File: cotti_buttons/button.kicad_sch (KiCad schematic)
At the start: 5 parts, among them SW1 SW_Push_Dual, U1 Invert Schmitt

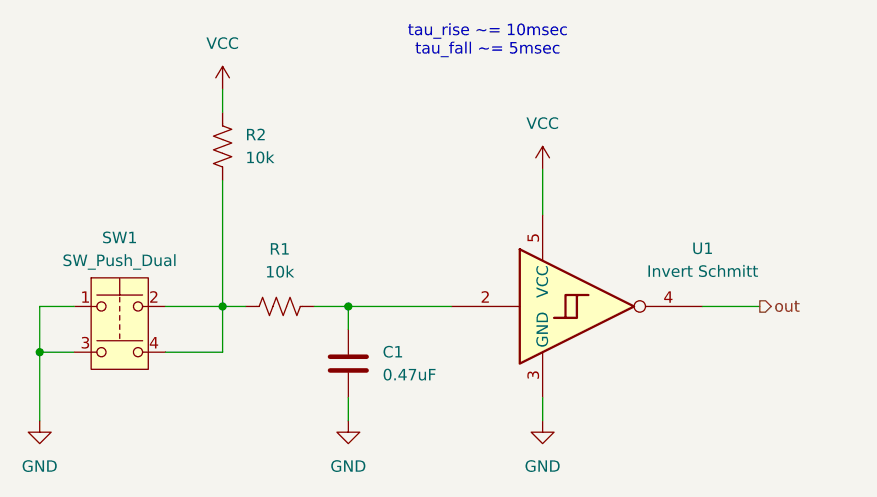
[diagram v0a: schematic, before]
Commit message: feat: cotti uttons with new libs
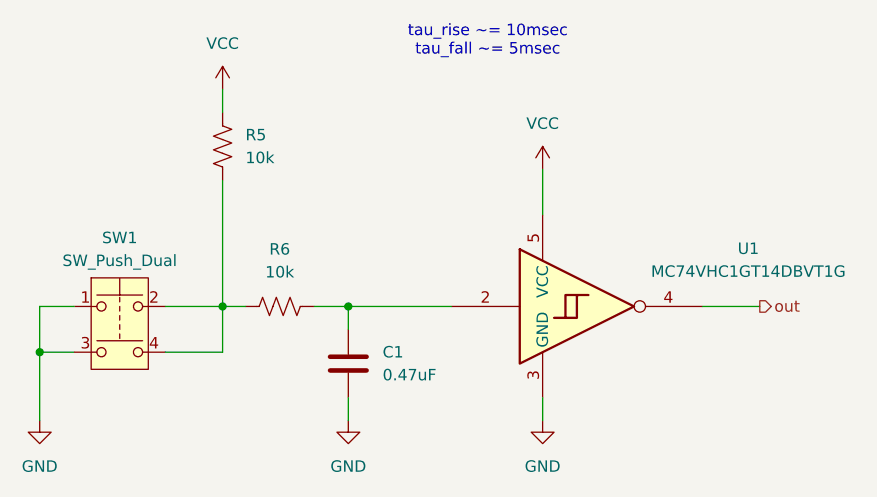
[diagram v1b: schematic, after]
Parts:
- removed SW1: SW_Push_Dual, Button_Switch_THT:SW_PUSH_6mm_H5mm, symbol Switch:SW_Push_Dual
- removed U1: Invert Schmitt, Package_TO_SOT_SMD:SC-74A-5_1.55x2.9mm_P0.95mm, symbol 74xGxx:74AHC1G14
- added SW1: SW_Push_Dual, Button_Switch_THT:SW_PUSH_6mm_H5mm, symbol cotti_switch:SW_Push_Dual
- added U1: MC74VHC1GT14DBVT1G, Package_TO_SOT_SMD:SC-74A-5_1.55x2.9mm_P0.95mm, symbol cotti_ic:inverter_schmitt_input
- renumbered R2 to R5, R1 to R6
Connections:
- net GND: now also SW1.1, SW1.3, U1.3 (GND)
- net VCC: now also U1.5 (VCC)
- net out: now also U1.4
- net at C1.1, R6.2: now also U1.2
- net at R5.2, R6.1: now also SW1.2, SW1.4
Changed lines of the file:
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@@
-	)
-	(symbol
-		(lib_id "74xGxx:74AHC1G14")
-		(at 173.99 97.79 0)
-		(unit 1)
-		(exclude_from_sim no)
-		(in_bom yes)
-		(on_board yes)
-		(dnp no)
-		(fields_autoplaced yes)
-		(property "Reference" "U1"
-			(at 186.69 91.3698 0)
-			(effects
-				(font
-					(size 1.27 1.27)
-				)
-			)
-		)
-		(property "Value" "Invert Schmitt"
-			(at 186.69 93.9098 0)
-			(effects
-				(font
-					(size 1.27 1.27)
-				)
-			)
-		)
-		(property "Footprint" "Package_TO_SOT_SMD:SC-74A-5_1.55x2.9mm_P0.95mm"
-			(at 173.99 97.79 0)
-			(effects
-				(font
-					(size 1.27 1.27)
-				)
-				(hide yes)
-			)
-		)
-		(property "Datasheet" "https://www.onsemi.com/pdf/datasheet/mc74vhc1g14-d.pdf"
-			(at 173.99 104.14 0)
-			(effects
-				(font
-					(size 1.27 1.27)
-				)
-				(justify left)
-				(hide yes)
-			)
-		)
-		(property "Description" "Inverter IC 1 Channel Schmitt Trigger SC-74A"
-			(at 173.99 97.79 0)
-			(effects
-				(font
-					(size 1.27 1.27)
-				)
-				(hide yes)
-			)
-		)
-		(property "Digikey" "https://www.digikey.com/en/products/detail/onsemi/MC74VHC1GT14DBVT1G/10064713"
-			(at 173.99 97.79 0)
-			(effects
-				(font
-					(size 1.27 1.27)
-				)
-				(hide yes)
-			)
-		)
-		(property "Digikey P/N" "488-MC74VHC1GT14DBVT1GCT-ND"
-			(at 173.99 97.79 0)
-			(effects
-				(font
-					(size 1.27 1.27)
-				)
-				(hide yes)
-			)
-		)
-		(property "Mfr." "onsemi"
-			(at 173.99 97.79 0)
-			(effects
-				(font
-					(size 1.27 1.27)
-				)
-				(hide yes)
-			)
-		)
-		(property "Mfr. P/N" "MC74VHC1GT14DBVT1G"
-			(at 173.99 97.79 0)
-			(effects
-				(font
-					(size 1.27 1.27)
-				)
-				(hide yes)
-			)
-		)
-		(pin "1"
-		)
-		(pin "4"
-		)
-		(pin "3"
-		)
-		(pin "2"
-		)
-		(pin "5"
-		)
-		(instances
-			(project "cotti_buttons"
-				(path "/673b428a-a10a-4837-8ece-1839a9ec4aa8/34456084-0fea-4792-bf42-1a35ca3e3257"
-					(reference "U1")
-					(unit 1)
-				)
-				(path "/673b428a-a10a-4837-8ece-1839a9ec4aa8/408eaa88-2d34-400c-9210-e43e7ee9c2ee"
-					(reference "U3")
-					(unit 1)
-				)
-				(path "/673b428a-a10a-4837-8ece-1839a9ec4aa8/5fd56874-714f-4976-9abd-9de7879c2a1d"
-					(reference "U4")
-					(unit 1)
-				)
-				(path "/673b428a-a10a-4837-8ece-1839a9ec4aa8/7882fe45-d505-43e1-b077-86683bbfd833"
-					(reference "U2")
-					(unit 1)
-				)
-			)
-		)
 	)
 	(symbol
@@
 		(dnp no)
 		(fields_autoplaced yes)
-		(property "Reference" "#PWR05"
+		(property "Reference" "#PWR03"
 			(at 113.03 116.84 0)
 			(effects
@@
 			(project "cotti_buttons"
 				(path "/673b428a-a10a-4837-8ece-1839a9ec4aa8/34456084-0fea-4792-bf42-1a35ca3e3257"
-					(reference "#PWR05")
+					(reference "#PWR03")
 					(unit 1)
 				)
@@
 		(dnp no)
 		(fields_autoplaced yes)
-		(property "Reference" "#PWR04"
+		(property "Reference" "#PWR05"
 			(at 147.32 116.84 0)
 			(effects
@@
 			(project ""
 				(path "/673b428a-a10a-4837-8ece-1839a9ec4aa8/34456084-0fea-4792-bf42-1a35ca3e3257"
-					(reference "#PWR04")
+					(reference "#PWR05")
 					(unit 1)
 				)
@@
 		(on_board yes)
 		(dnp no)
-		(property "Reference" "R2"
+		(property "Reference" "R5"
 			(at 135.89 78.7399 0)
 			(effects
@@
 			(project "cotti_buttons"
 				(path "/673b428a-a10a-4837-8ece-1839a9ec4aa8/34456084-0fea-4792-bf42-1a35ca3e3257"
-					(reference "R2")
+					(reference "R5")
 					(unit 1)
 				)
 				(path "/673b428a-a10a-4837-8ece-1839a9ec4aa8/408eaa88-2d34-400c-9210-e43e7ee9c2ee"
-					(reference "R6")
+					(reference "R9")
 					(unit 1)
 				)
 				(path "/673b428a-a10a-4837-8ece-1839a9ec4aa8/5fd56874-714f-4976-9abd-9de7879c2a1d"
-					(reference "R8")
+					(reference "R11")
 					(unit 1)
 				)
 				(path "/673b428a-a10a-4837-8ece-1839a9ec4aa8/7882fe45-d505-43e1-b077-86683bbfd833"
-					(reference "R4")
+					(reference "R7")
 					(unit 1)
 				)
@@
 		(dnp no)
 		(fields_autoplaced yes)
-		(property "Reference" "#PWR03"
+		(property "Reference" "#PWR04"
 			(at 133.35 77.47 0)
 			(effects
@@
 			(project "cotti_buttons"
 				(path "/673b428a-a10a-4837-8ece-1839a9ec4aa8/34456084-0fea-4792-bf42-1a35ca3e3257"
-					(reference "#PWR03")
+					(reference "#PWR04")
 					(unit 1)
 				)
@@
 	)
 	(symbol
-		(lib_id "Switch:SW_Push_Dual")
+		(lib_id "cotti_ic:inverter_schmitt_input")
+		(at 173.99 97.79 0)
+		(unit 1)
+		(exclude_from_sim no)
+		(in_bom yes)
+		(on_board yes)
+		(dnp no)
+		(fields_autoplaced yes)
+		(property "Reference" "U1"
+			(at 191.77 91.3698 0)
+			(effects
+				(font
+					(size 1.27 1.27)
+				)
+			)
+		)
+		(property "Value" "MC74VHC1GT14DBVT1G"
+			(at 191.77 93.9098 0)
+			(effects
+				(font
+					(size 1.27 1.27)
+				)
+			)
+		)
+		(property "Footprint" "Package_TO_SOT_SMD:SC-74A-5_1.55x2.9mm_P0.95mm"
+			(at 170.434 69.596 0)
+			(effects
+				(font
+					(size 1.27 1.27)
+				)
+				(hide yes)
+			)
+		)
+		(property "Datasheet" "https://www.onsemi.com/pdf/datasheet/mc74vhc1g14-d.pdf"
+			(at 139.192 62.23 0)
+			(effects
+				(font
+					(size 1.27 1.27)
+				)
+				(justify left)
+				(hide yes)
+			)
+		)
+		(property "Description" "Inverter IC 1 Channel Schmitt Trigger SC-74A Push-Pull output"
+			(at 170.942 65.024 0)
+			(effects
+				(font
+					(size 1.27 1.27)
+				)
+				(hide yes)
+			)
+		)
+		(property "Digikey" "https://www.digikey.com/en/products/detail/onsemi/MC74VHC1GT14DBVT1G/10064713"
+			(at 172.212 72.898 0)
+			(effects
+				(font
+					(size 1.27 1.27)
+				)
+				(hide yes)
+			)
+		)
+		(property "Mfr." "onsemi"
+			(at 172.974 55.88 0)
+			(effects
+				(font
+					(size 1.27 1.27)
+				)
+				(hide yes)
+			)
+		)
+		(property "Mfr. P/N" "MC74VHC1GT14DBVT1G"
+			(at 172.466 58.42 0)
+			(effects
+				(font
+					(size 1.27 1.27)
+				)
+				(hide yes)
+			)
+		)
+		(pin "5"
+		)
+		(pin "3"
+		)
+		(pin "1"
+		)
+		(pin "4"
+		)
+		(pin "2"
+		)
+		(instances
+			(project ""
+				(path "/673b428a-a10a-4837-8ece-1839a9ec4aa8/34456084-0fea-4792-bf42-1a35ca3e3257"
+					(reference "U1")
+					(unit 1)
+				)
+				(path "/673b428a-a10a-4837-8ece-1839a9ec4aa8/408eaa88-2d34-400c-9210-e43e7ee9c2ee"
+					(reference "U3")
+					(unit 1)
+				)
+				(path "/673b428a-a10a-4837-8ece-1839a9ec4aa8/5fd56874-714f-4976-9abd-9de7879c2a1d"
+					(reference "U4")
+					(unit 1)
+				)
+				(path "/673b428a-a10a-4837-8ece-1839a9ec4aa8/7882fe45-d505-43e1-b077-86683bbfd833"
+					(reference "U2")
+					(unit 1)
+				)
+			)
+		)
+	)
+	(symbol
+		(lib_id "cotti_switch:SW_Push_Dual")
 		(at 121.92 100.33 0)
 		(unit 1)
@@
 		)
 		(property "Footprint" "Button_Switch_THT:SW_PUSH_6mm_H5mm"
-			(at 121.92 92.71 0)
-			(effects
-				(font
-					(size 1.27 1.27)
-				)
-				(hide yes)
-			)
-		)
-		(property "Datasheet" "https://www.cuidevices.com/product/resource/ts02.pdf"
-			(at 121.92 100.33 0)
+			(at 120.142 68.072 0)
+			(effects
+				(font
+					(size 1.27 1.27)
+				)
+				(hide yes)
+			)
+		)
+		(property "Datasheet" "https://www.sameskydevices.com/product/resource/ts02.pdf"
+			(at 120.396 83.312 0)
 			(effects
 				(font
@@
 		)
 		(property "Description" "Tactile Switch SPST-NO Top Actuated Through Hole"
-			(at 121.92 100.33 0)
+			(at 121.158 87.63 0)
 			(effects
 				(font
@@
 		)
 		(property "Digikey" "https://www.digikey.com/en/products/detail/same-sky-formerly-cui-devices/TS02-66-60-BK-260-SCR-D/15634288"
-			(at 121.92 100.33 0)
-			(effects
-				(font
-					(size 1.27 1.27)
-				)
-				(hide yes)
-			)
-		)
-		(property "Digikey P/N" "2223-TS02-66-60-BK-260-SCR-D-ND"
-			(at 121.92 100.33 0)
+			(at 124.46 79.248 0)
 			(effects
 				(font
@@
 		)
 		(property "Mfr." "Same Sky (Formerly CUI Devices)"
-			(at 121.92 100.33 0)
+			(at 122.428 72.644 0)
 			(effects
 				(font
@@
 		)
 		(property "Mfr. P/N" "TS02-66-60-BK-260-SCR-D"
-			(at 121.92 100.33 0)
-			(effects
-				(font
-					(size 1.27 1.27)
-				)
-				(hide yes)
-			)
+			(at 121.92 75.438 0)
+			(effects
+				(font
+					(size 1.27 1.27)
+				)
+				(hide yes)
+			)
+		)
+		(pin "2"
+		)
+		(pin "4"
+		)
+		(pin "3"
 		)
 		(pin "1"
-		)
-		(pin "2"
-		)
-		(pin "3"
-		)
-		(pin "4"
 		)
 		(instances
@@
 		(dnp no)
 		(fields_autoplaced yes)
-		(property "Reference" "R1"
+		(property "Reference" "R6"
 			(at 139.7 91.44 90)
 			(effects
@@
 			(project "cotti_buttons"
 				(path "/673b428a-a10a-4837-8ece-1839a9ec4aa8/34456084-0fea-4792-bf42-1a35ca3e3257"
-					(reference "R1")
+					(reference "R6")
 					(unit 1)
 				)
 				(path "/673b428a-a10a-4837-8ece-1839a9ec4aa8/408eaa88-2d34-400c-9210-e43e7ee9c2ee"
-					(reference "R5")
+					(reference "R10")
 					(unit 1)
 				)
 				(path "/673b428a-a10a-4837-8ece-1839a9ec4aa8/5fd56874-714f-4976-9abd-9de7879c2a1d"
-					(reference "R7")
+					(reference "R12")
 					(unit 1)
 				)
 				(path "/673b428a-a10a-4837-8ece-1839a9ec4aa8/7882fe45-d505-43e1-b077-86683bbfd833"
-					(reference "R3")
-					(unit 1)
-				)
+					(reference "R8")
+					(unit 1)
+				)

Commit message: feat: cotti buttons gerber files
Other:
- company: (none) -> Cotti
- title: Cotti Button Module -> Button Module
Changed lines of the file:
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@@
 	(paper "A4")
 	(title_block
-		(title "Cotti Button Module")
-		(date "2025-12-18")
+		(title "Button Module")
+		(date "2026-01-17")
 		(rev "0.0")
+		(company "Cotti")
 	)
 	(text "tau_rise ~= 10msec\ntau_fall ~= 5msec"
